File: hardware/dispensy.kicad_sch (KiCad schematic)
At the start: 3 parts, among them U14 USB-A, U15 DBT50G-7_62-4P

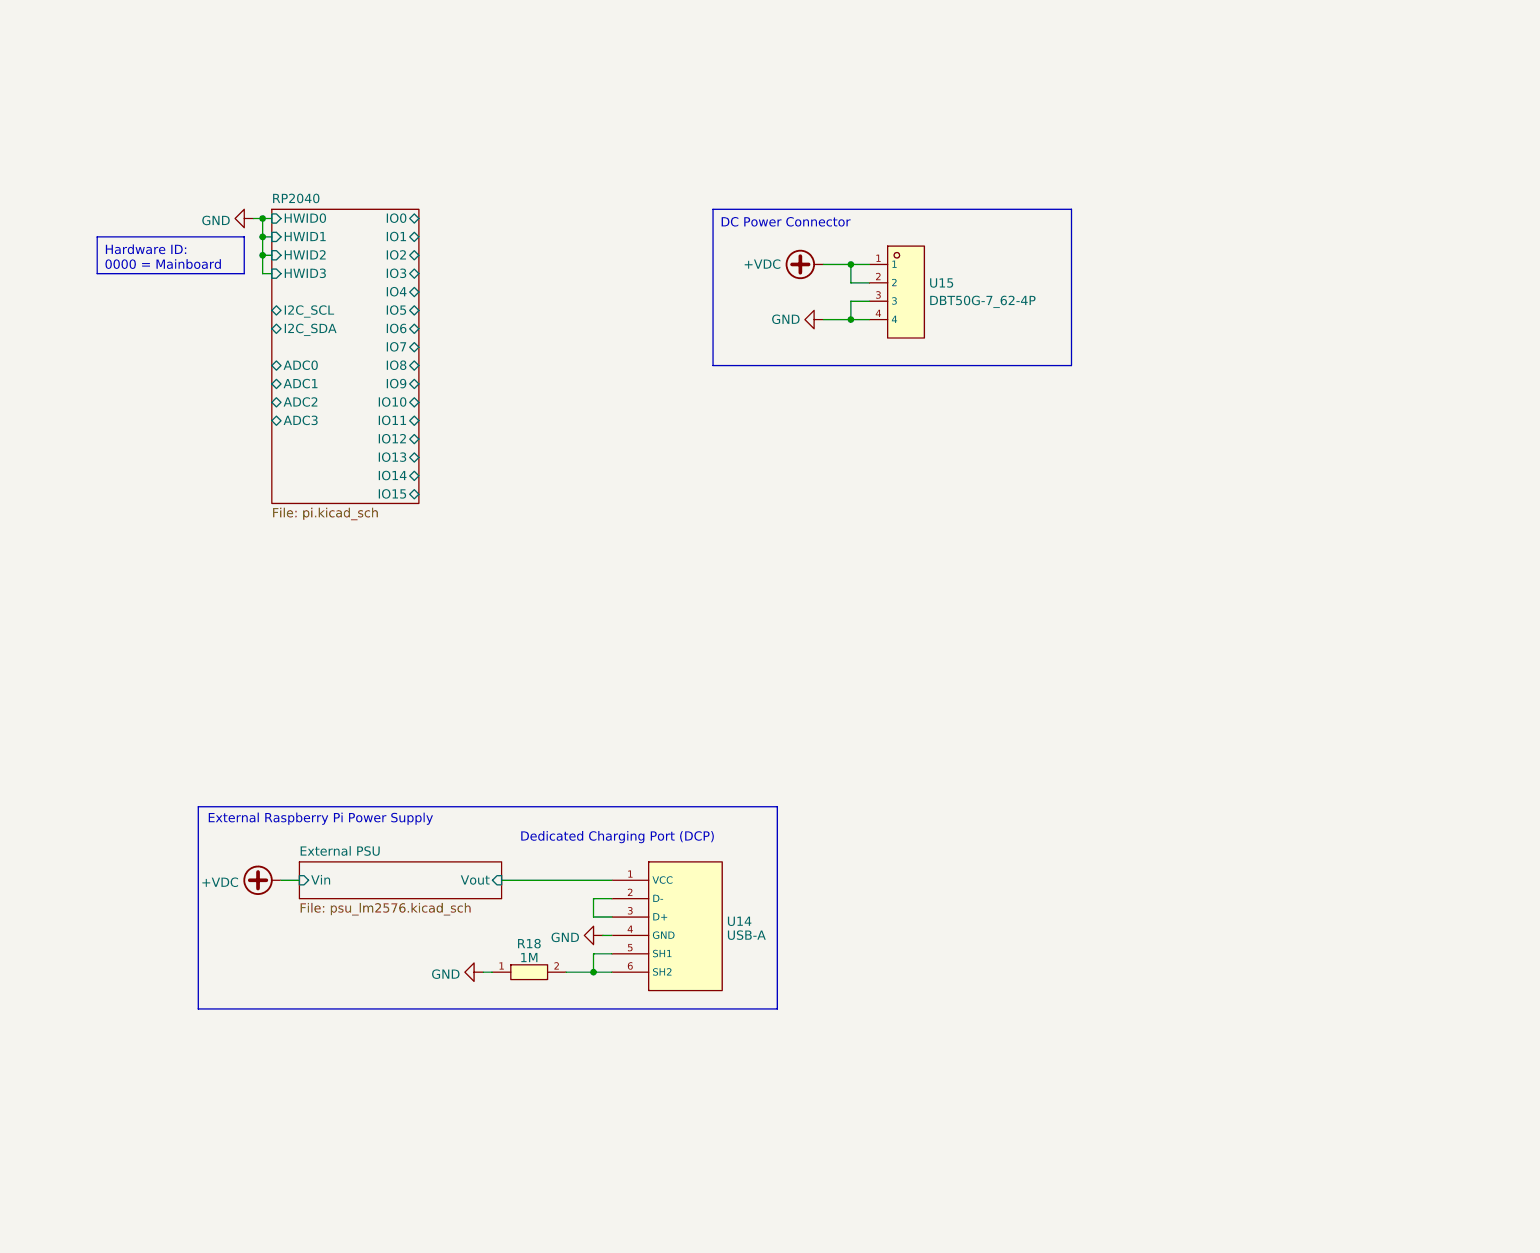
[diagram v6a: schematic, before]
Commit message: start working on mainboard pcb layout
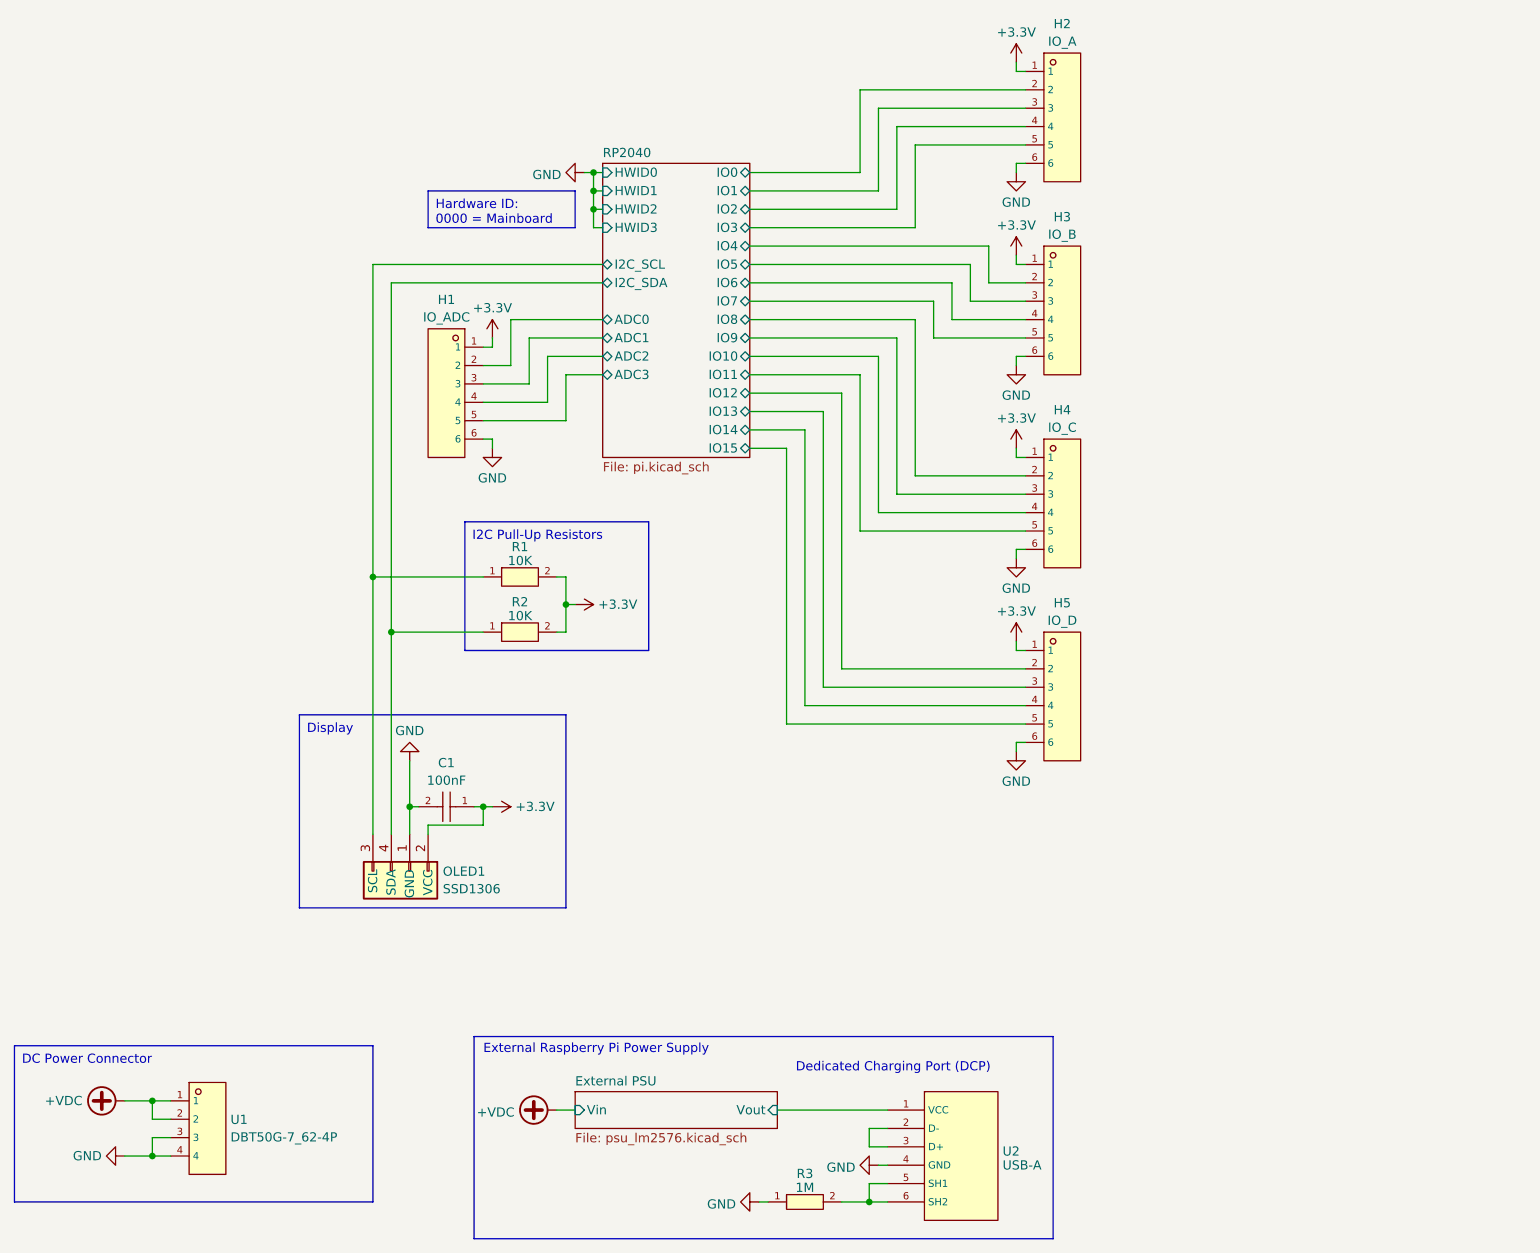
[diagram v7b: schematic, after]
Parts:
- added C1: 100nF, jlc_footprints:C0402, symbol jlc:CC0402KRX7R8BB104
- added H1: IO_ADC, jlc_footprints:HDR-TH_6P-P2.54-V-F, symbol jlc:Header-Female-2_54_1x6
- added H2: IO_A, jlc_footprints:HDR-TH_6P-P2.54-V-F, symbol jlc:Header-Female-2_54_1x6
- added H3: IO_B, jlc_footprints:HDR-TH_6P-P2.54-V-F, symbol jlc:Header-Female-2_54_1x6
- added H4: IO_C, jlc_footprints:HDR-TH_6P-P2.54-V-F, symbol jlc:Header-Female-2_54_1x6
- added H5: IO_D, jlc_footprints:HDR-TH_6P-P2.54-V-F, symbol jlc:Header-Female-2_54_1x6
- added OLED1: SSD1306, extern:SSD1306_0.96_Oled, symbol SSD1306:SSD1306
- added R1, R2: 10K, jlc_footprints:R0402, symbol jlc:CR-02FL6---10K
- renumbered R18 to R3, U15 to U1, U14 to U2
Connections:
- net GND: now also C1.2, H1.6, H2.6, H3.6, H4.6, H5.6, OLED1.1 (GND)
- net RP2040/ADC0: now also H1.2
- net RP2040/ADC1: now also H1.3
- net RP2040/ADC2: now also H1.4
- net RP2040/ADC3: now also H1.5
- net RP2040/I2C_SCL: now also OLED1.3 (SCL), R1.1
- net RP2040/I2C_SDA: now also OLED1.4 (SDA), R2.1
- net RP2040/IO0: now also H2.2
- net RP2040/IO1: now also H2.3
- net RP2040/IO10: now also H4.4
- net RP2040/IO11: now also H4.5
- net RP2040/IO12: now also H5.2
- net RP2040/IO13: now also H5.3
- net RP2040/IO14: now also H5.4
- net RP2040/IO15: now also H5.5
- net RP2040/IO2: now also H2.4
- net RP2040/IO3: now also H2.5
- net RP2040/IO4: now also H3.2
- net RP2040/IO5: now also H3.3
- net RP2040/IO6: now also H3.4
- net RP2040/IO7: now also H3.5
- net RP2040/IO8: now also H4.2
- net RP2040/IO9: now also H4.3
- new net +3.3V: C1.1, H1.1, H2.1, H3.1, H4.1, H5.1, OLED1.2 (VCC), R1.2, R2.2
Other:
- moved on the sheet: R3, U1, U2

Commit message: More routing for power and can stuff
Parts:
- added H11, H12, H13, H14: MountingHole, MountingHole:MountingHole_3.2mm_M3_Pad_TopBottom, symbol Mechanical:MountingHole
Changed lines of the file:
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@@
     (effects (font (size 1.27 1.27)) (justify left bottom))
+  )
+  (symbol (lib_id "Mechanical:MountingHole") (at 215.9 147.32 0) (unit 1)
+    (in_bom yes) (on_board yes) (dnp no) (fields_autoplaced)
+    (property "Reference" "H11" (at 218.44 146.1079 0)
+      (effects (font (size 1.27 1.27)) (justify left))
+    )
+    (property "Value" "MountingHole" (at 218.44 148.5321 0)
+      (effects (font (size 1.27 1.27)) (justify left))
+    )
+    (property "Footprint" "MountingHole:MountingHole_3.2mm_M3_Pad_TopBottom" (at 215.9 147.32 0)
+      (effects (font (size 1.27 1.27)) hide)
+    )
+    (property "Datasheet" "~" (at 215.9 147.32 0)
+      (effects (font (size 1.27 1.27)) hide)
+    )
+    (instances
+      (project "dispensy"
+        (path "/a50b51f9-900f-4bbb-8934-4acbc429c37b"
+          (reference "H11") (unit 1)
+        )
+      )
+    )
   )
   (symbol (lib_id "power:+3.3V") (at 163.83 82.55 0) (unit 1)
@@
         (path "/a50b51f9-900f-4bbb-8934-4acbc429c37b"
           (reference "#PWR011") (unit 1)
+        )
+      )
+    )
+  )
+  (symbol (lib_id "Mechanical:MountingHole") (at 215.9 157.48 0) (unit 1)
+    (in_bom yes) (on_board yes) (dnp no) (fields_autoplaced)
+    (property "Reference" "H13" (at 218.44 156.2679 0)
+      (effects (font (size 1.27 1.27)) (justify left))
+    )
+    (property "Value" "MountingHole" (at 218.44 158.6921 0)
+      (effects (font (size 1.27 1.27)) (justify left))
+    )
+    (property "Footprint" "MountingHole:MountingHole_3.2mm_M3_Pad_TopBottom" (at 215.9 157.48 0)
+      (effects (font (size 1.27 1.27)) hide)
+    )
+    (property "Datasheet" "~" (at 215.9 157.48 0)
+      (effects (font (size 1.27 1.27)) hide)
+    )
+    (instances
+      (project "dispensy"
+        (path "/a50b51f9-900f-4bbb-8934-4acbc429c37b"
+          (reference "H13") (unit 1)
         )
       )
@@
     )
   )
+  (symbol (lib_id "Mechanical:MountingHole") (at 215.9 152.4 0) (unit 1)
+    (in_bom yes) (on_board yes) (dnp no) (fields_autoplaced)
+    (property "Reference" "H12" (at 218.44 151.1879 0)
+      (effects (font (size 1.27 1.27)) (justify left))
+    )
+    (property "Value" "MountingHole" (at 218.44 153.6121 0)
+      (effects (font (size 1.27 1.27)) (justify left))
+    )
+    (property "Footprint" "MountingHole:MountingHole_3.2mm_M3_Pad_TopBottom" (at 215.9 152.4 0)
+      (effects (font (size 1.27 1.27)) hide)
+    )
+    (property "Datasheet" "~" (at 215.9 152.4 0)
+      (effects (font (size 1.27 1.27)) hide)
+    )
+    (instances
+      (project "dispensy"
+        (path "/a50b51f9-900f-4bbb-8934-4acbc429c37b"
+          (reference "H12") (unit 1)
+        )
+      )
+    )
+  )
   (symbol (lib_id "jlc:DBT50G-7_62-4P") (at 52.07 176.53 0) (unit 1)
     (in_bom yes) (on_board yes) (dnp no) (fields_autoplaced)
@@
         )
       )
+    )
+  )
+  (symbol (lib_id "Mechanical:MountingHole") (at 215.9 162.56 0) (unit 1)
+    (in_bom yes) (on_board yes) (dnp no) (fields_autoplaced)
+    (property "Reference" "H14" (at 218.44 161.3479 0)
+      (effects (font (size 1.27 1.27)) (justify left))
+    )
+    (property "Value" "MountingHole" (at 218.44 163.7721 0)
+      (effects (font (size 1.27 1.27)) (justify left))
+    )
+    (property "Footprint" "MountingHole:MountingHole_3.2mm_M3_Pad_TopBottom" (at 215.9 162.56 0)
+      (effects (font (size 1.27 1.27)) hide)
+    )
+    (property "Datasheet" "~" (at 215.9 162.56 0)
+      (effects (font (size 1.27 1.27)) hide)
+    )
+    (instances
+      (project "dispensy"
+        (path "/a50b51f9-900f-4bbb-8934-4acbc429c37b"
+          (reference "H14") (unit 1)
+        )
+      )
